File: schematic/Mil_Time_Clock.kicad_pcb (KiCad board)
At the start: 2 copper layers, 188.7 x 101.1 mm, 105 parts, among them J1 Conn_01x27, J2 Speaker_Conn_01x02, J3 Barrel_Jack_Switch, J4 Conn_01x27, Q1 2N3904, Q2 2N3904, Q3 2N3904, Q4 2N3904, Q5 2N3904, U1 SM420561N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

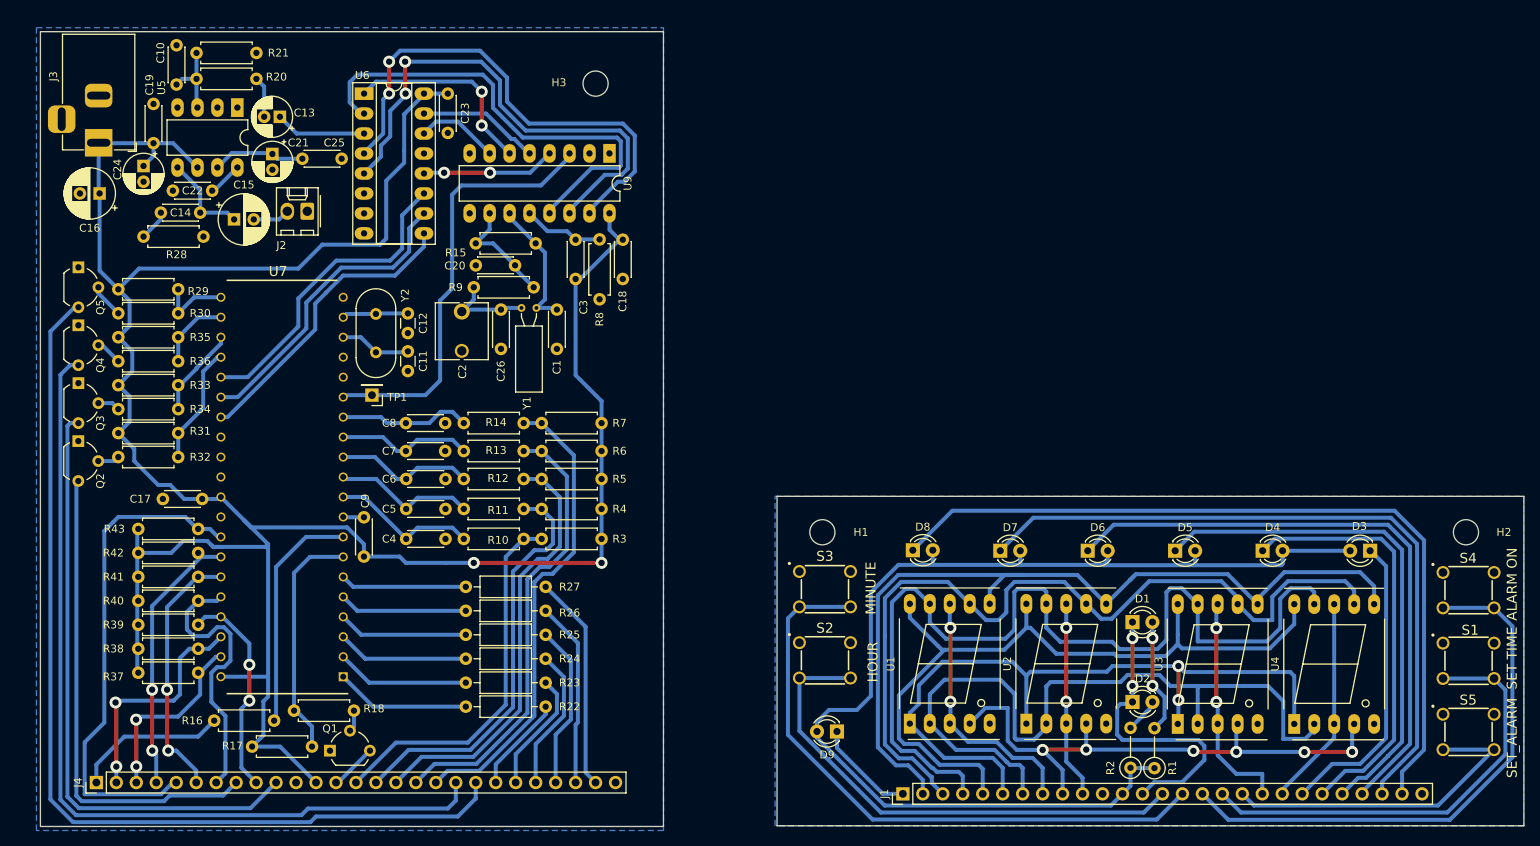
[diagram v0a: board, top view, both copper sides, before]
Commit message: adjusted a trace, since ISOPRO did not pick up on it being 12 mil away.
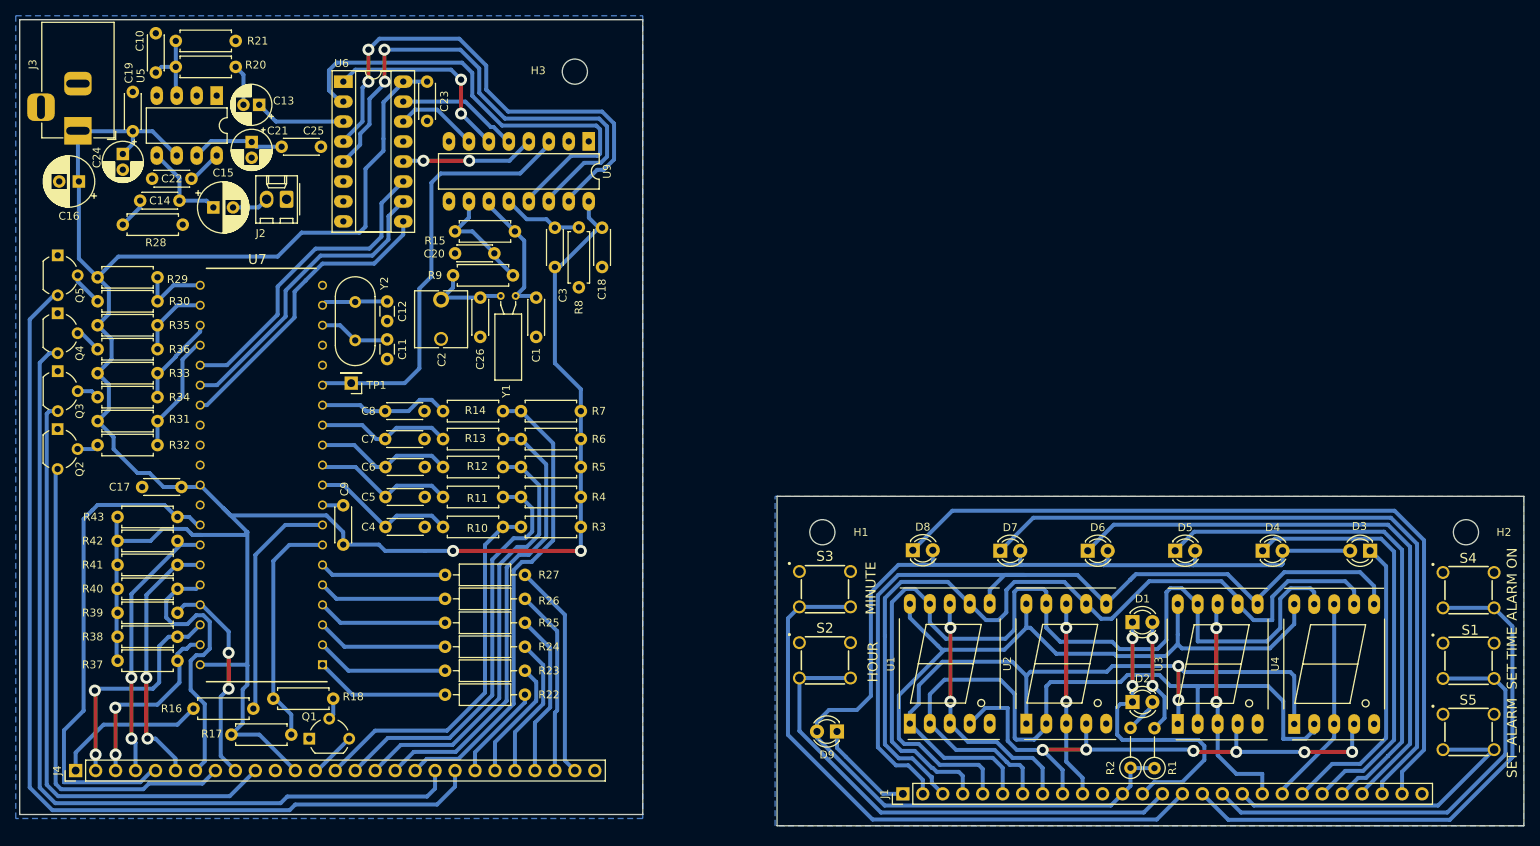
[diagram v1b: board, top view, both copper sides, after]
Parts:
- moved H3 3.04 mm to (131.1, 38.6)
- moved J4 3.04 mm to (67.6, 127.5)
- moved C13 3.04 mm to (90.9, 42.8)
- moved C17 3.04 mm to (81.0, 91.4)
- moved C19 3.04 mm to (74.8, 46.2)
- moved C20 3.04 mm to (115.8, 61.7)
- moved C23 3.04 mm to (112.3, 39.9)
- moved C24 3.04 mm to (73.6, 49.1)
- moved C7 3.04 mm to (106.9, 85.3)
- moved C8 3.04 mm to (106.9, 81.8)
- moved C9 3.04 mm to (101.6, 98.8)
- moved J2 3.04 mm to (94.4, 54.8)
- moved J3 3.04 mm to (67.9, 46.1)
- moved Q1 3.04 mm to (97.3, 123.5)
- moved Q2 3.04 mm to (65.3, 84.1)
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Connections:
- C10 pad 1: Net-(C10-Pad1) -> (no net)
- C13 pad 1: Net-(C13-Pad1) -> (no net)
- C21 pad 1: Net-(C21-Pad1) -> (no net)
- C22 pad 2: Net-(C22-Pad2) -> (no net)
- C25 pad 1: Net-(C21-Pad1) -> (no net)
- R20 pad 1: Net-(C10-Pad1) -> (no net)
- R21 pad 2: Net-(C10-Pad1) -> (no net)
- U5 pad 3: Net-(C10-Pad1) -> (no net)
- U5 pad 7: Net-(C21-Pad1) -> (no net)
- U5 pad 8: Net-(C22-Pad2) -> (no net)
- U6 pad 3: Net-(C13-Pad1) -> (no net)
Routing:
- net (no net): track 0.00 -> 37.6 mm
- net Net-(C21-Pad1): track 11.7 -> 0.00 mm
- net Net-(C13-Pad1): track 11.6 -> 0.00 mm
- net Net-(C10-Pad1): track 9.84 -> 0.00 mm
- net Net-(C22-Pad2): track 4.43 -> 0.00 mm
- net /MCU_BOARD/A: track 23.7 -> 24.9 mm
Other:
- board size 188.7 x 101.1 mm -> 191.3 x 102.5 mm

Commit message: whoops, wrong trace, now the 12 mil trace is adjusted
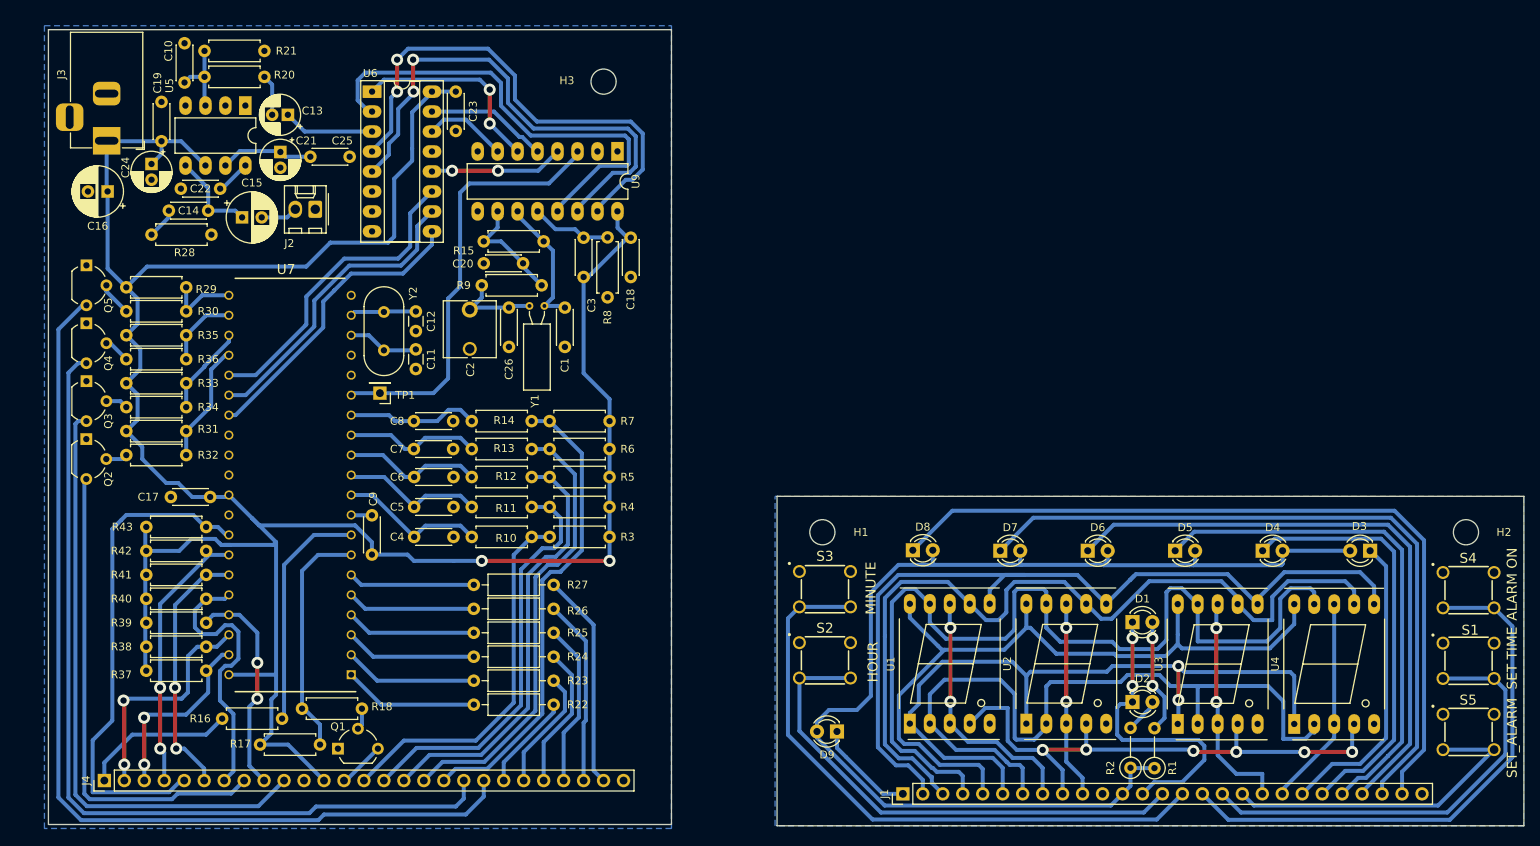
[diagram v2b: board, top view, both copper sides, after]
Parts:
- moved C1 3.87 mm to (129.8, 73.6)
- moved R22 3.87 mm to (128.4, 119.1)
- moved R29 3.87 mm to (81.6, 66.0)
- moved R32 3.87 mm to (81.6, 87.4)
- moved C3 3.87 mm to (132.2, 64.7)
- moved H3 3.87 mm to (134.7, 39.9)
- moved U9 3.87 mm to (136.5, 48.8)
- moved C10 3.87 mm to (81.4, 40.0)
- moved C17 3.87 mm to (84.7, 92.7)
- moved C19 3.87 mm to (78.5, 47.5)
- moved C9 3.87 mm to (105.3, 100.0)
- moved J4 3.87 mm to (71.2, 128.8)
- moved Q1 3.87 mm to (100.9, 124.7)
- moved Q2 3.87 mm to (68.9, 85.3)
- moved R18 3.87 mm to (96.4, 119.6)
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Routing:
- net /MCU_BOARD/C: track 27.0 -> 27.6 mm
- net /MCU_BOARD/A: track 24.9 -> 24.4 mm
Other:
- board size 191.3 x 102.5 mm -> 187.7 x 101.3 mm

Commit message: added padding resistor to halve the speaker volume and deal with some noise issues in some units. Noise is originating from the 7 segment LED data lines. It runs at about 1khz so this makes sense, will try some software fixes in the future.
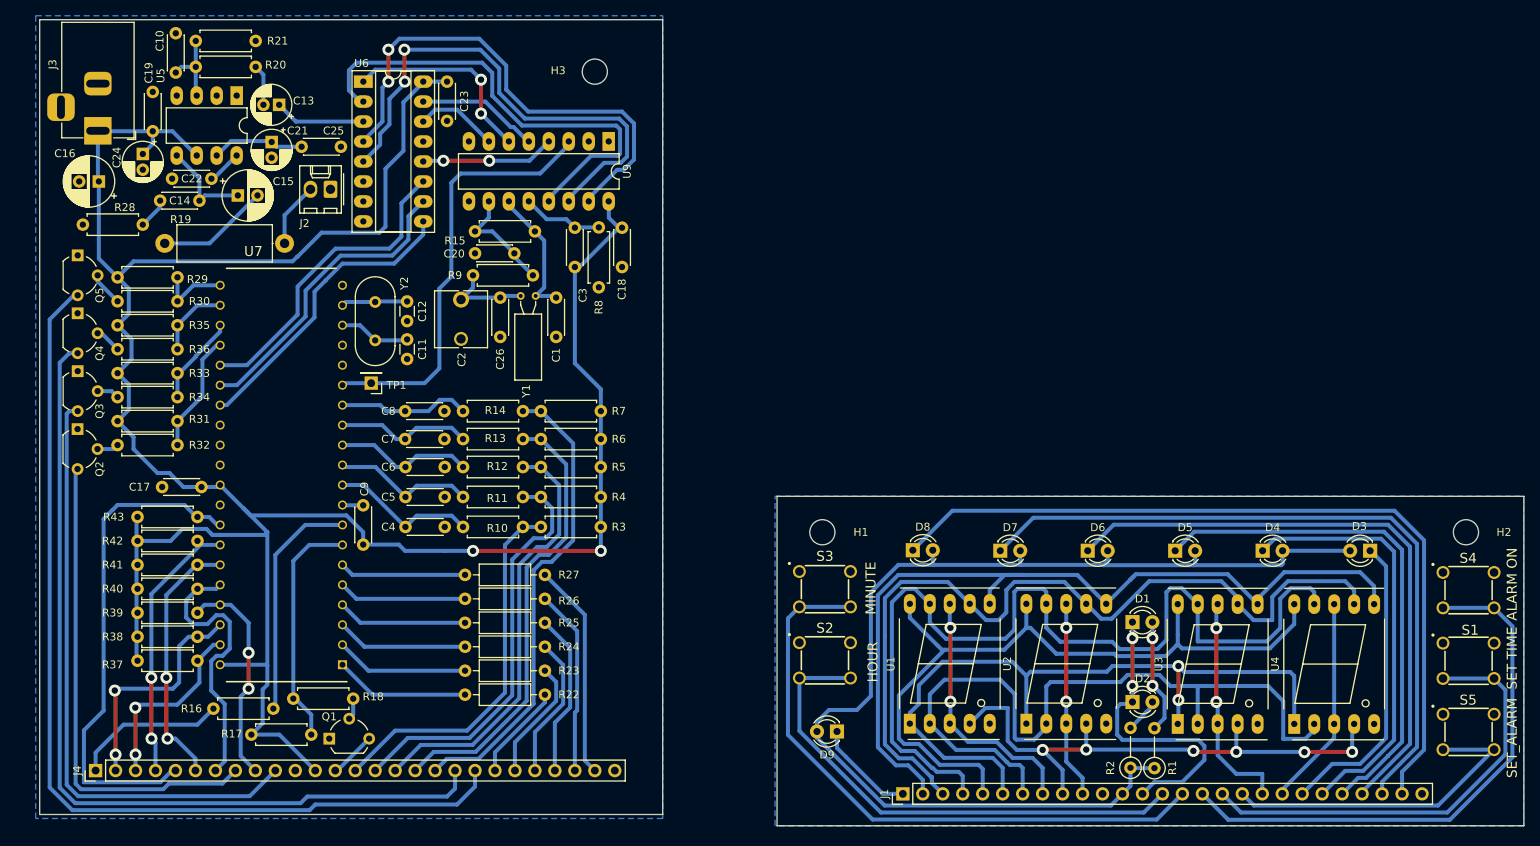
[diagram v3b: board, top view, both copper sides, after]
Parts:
- added R19: 8R_OPT, Resistor_THT:R_Axial_DIN0414_L11.9mm_D4.5mm_P15.24mm_Horizontal, F.Cu at (94.1, 60.5)
- C1: value 12pF -> 47pF
- C2: value 5-20pF -> 6-30pF
- C26: value 12pF -> 18pF
- moved J2 3.19 mm to (100.0, 53.6)
- moved C15 2.84 mm to (88.2, 54.4)
- moved C1 1.69 mm to (128.7, 72.3)
- moved C3 1.69 mm to (131.1, 63.5)
- moved U9 1.69 mm to (135.4, 47.5)
- moved C12 1.69 mm to (109.7, 67.8)
- moved C26 1.69 mm to (121.6, 67.3)
- moved C4 1.69 mm to (109.5, 96.5)
- moved C5 1.69 mm to (109.5, 92.7)
- moved R10 1.69 mm to (124.5, 96.5)
- moved R13 1.69 mm to (124.5, 85.3)
- moved R14 1.69 mm to (124.5, 81.8)
- moved R22 1.69 mm to (127.3, 117.9)
- moved R29 1.69 mm to (80.5, 64.8)
- moved R3 1.69 mm to (126.7, 96.5)
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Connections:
- C10 pad 1: (no net) -> Net-(C10-Pad1)
- C13 pad 1: (no net) -> Net-(C13-Pad1)
- C21 pad 1: (no net) -> Net-(C21-Pad1)
- C22 pad 2: (no net) -> Net-(C22-Pad2)
- C25 pad 1: (no net) -> Net-(C21-Pad1)
- J2 pad 2: Net-(C15-Pad2) -> Net-(J2-Pad2)
- R20 pad 1: (no net) -> Net-(C10-Pad1)
- R21 pad 2: (no net) -> Net-(C10-Pad1)
- U5 pad 3: (no net) -> Net-(C10-Pad1)
- U5 pad 7: (no net) -> Net-(C21-Pad1)
- U5 pad 8: (no net) -> Net-(C22-Pad2)
- U6 pad 3: (no net) -> Net-(C13-Pad1)
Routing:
- net (no net): track 37.6 -> 0.00 mm
- net Net-(C21-Pad1): track 0.00 -> 11.7 mm
- net Net-(C13-Pad1): track 0.00 -> 11.6 mm
- net Net-(C10-Pad1): track 0.00 -> 9.84 mm
- net Net-(C15-Pad2): track 4.70 -> 14.3 mm
- net Net-(J2-Pad2): track 0.00 -> 8.25 mm
- net Net-(C22-Pad2): track 0.00 -> 4.43 mm
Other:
- board size 187.7 x 101.3 mm -> 188.8 x 102.5 mm
